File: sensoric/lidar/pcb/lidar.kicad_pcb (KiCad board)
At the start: 2 copper layers, 51.4 x 48.3 mm, 19 parts, among them J1 TWI, J2 TFMini-Plus, J3 28BYJ-48, SW1 SW_Push, U1 ATmega8L-8PU, U2 ULN2003A, Y1 16 MHz

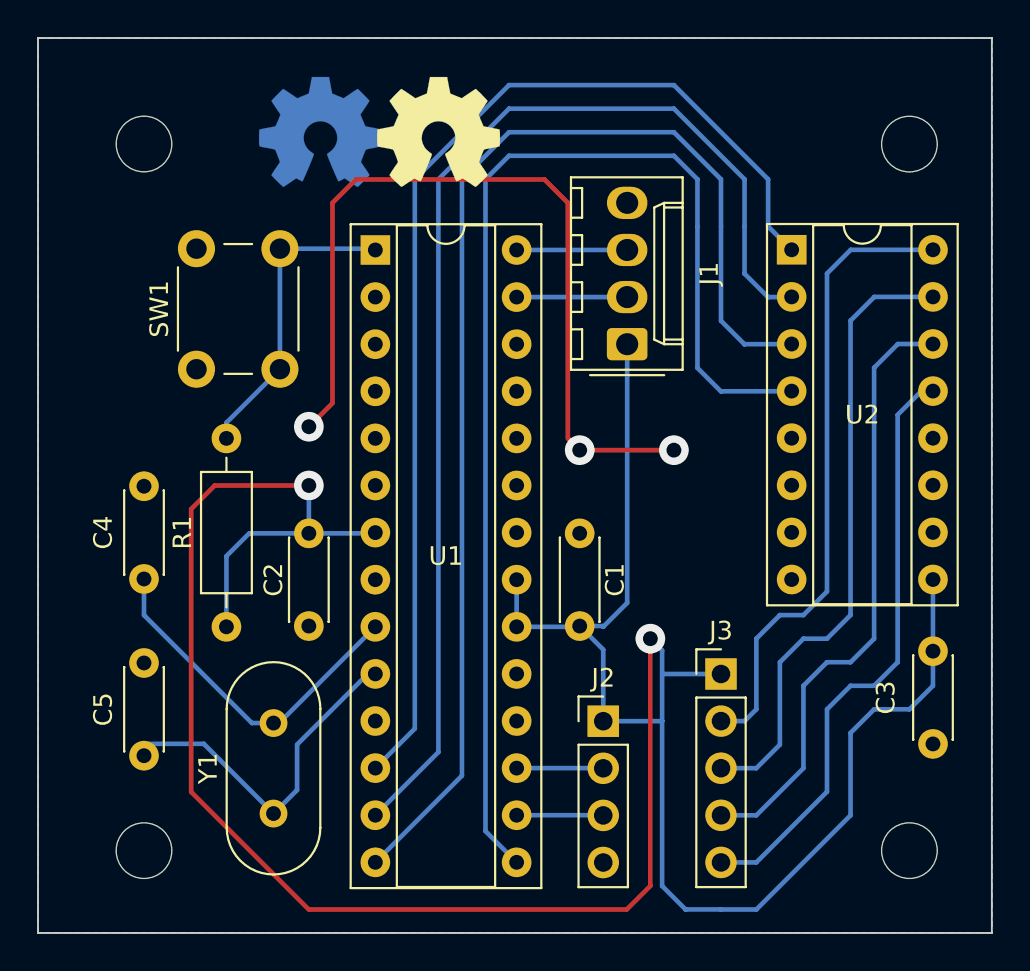
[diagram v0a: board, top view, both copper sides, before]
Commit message: refactor: moved from stepper motor to servo
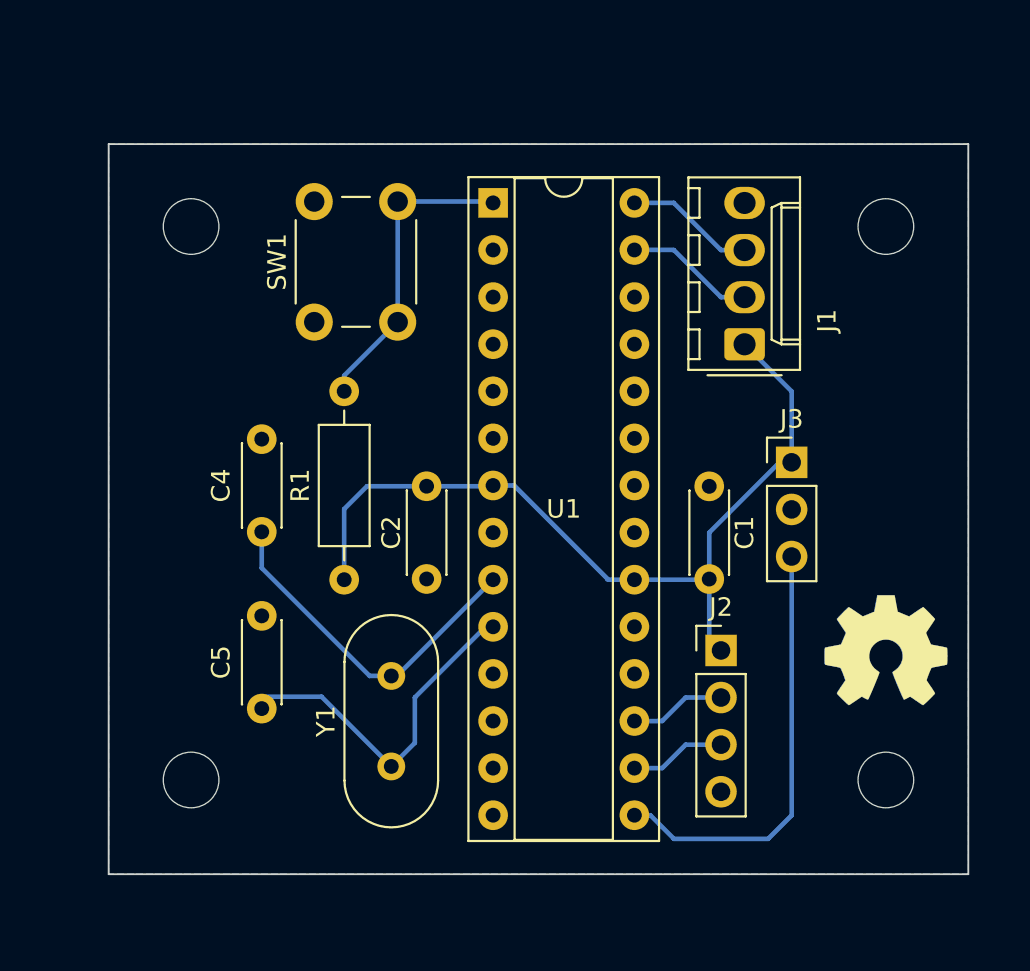
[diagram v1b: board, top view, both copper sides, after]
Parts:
- removed C3: 100 nF, Capacitor_THT:C_Disc_D4.3mm_W1.9mm_P5.00mm
- removed U2: ULN2003A, Package_DIP:DIP-16_W7.62mm_Socket
- J3: value 28BYJ-48 -> Servo SG90; footprint Connector_PinHeader_2.54mm:PinHeader_1x05_P2.54mm_Vertical -> Connector_PinHeader_2.54mm:PinHeader_1x03_P2.54mm_Vertical
- moved OSHW - copper 41.4 mm to (95.2, 95.2)
- moved OSHW - silk 36.9 mm to (95.2, 95.2)
- moved J3 12.0 mm to (90.2, 85.1)
- moved C1 7.43 mm to (85.7, 91.4)
- moved J2 7.41 mm to (86.4, 95.2)
- moved R1 6.84 mm to (66.0, 91.4)
- moved Y1 6.84 mm to (68.6, 101.5)
- moved C4 6.84 mm to (61.6, 88.9)
- moved C5 6.84 mm to (61.6, 98.4)
- moved C2 6.84 mm to (70.5, 86.4)
- moved U1 6.84 mm to (74.1, 71.1)
- moved SW1 6.84 mm to (64.4, 77.5)
- moved J1 6.33 mm to (87.6, 78.7)
- moved REF1 5.12 mm to (57.8, 72.4)
- moved REF2 4.62 mm to (95.2, 72.4)
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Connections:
- J3 pad 2: Net-(J3-Pad2) -> GND
- J3 pad 3: Net-(J3-Pad3) -> Net-(U1-Pad15)
- U1 pad 12: Net-(U1-Pad12) -> unconnected-(U1-Pad12)
- U1 pad 13: Net-(U1-Pad13) -> unconnected-(U1-Pad13)
- U1 pad 14: Net-(U1-Pad14) -> unconnected-(U1-Pad14)
- U1 pad 21: +5V -> unconnected-(U1-Pad21)
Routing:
- net +5V: track 155.4 -> 46.1 mm, vias 2 -> 0
- net Net-(U1-Pad14): track 66.8 -> 0.00 mm
- net Net-(U1-Pad13): track 63.5 -> 0.00 mm
- net Net-(U1-Pad12): track 60.2 -> 0.00 mm
- net GND: track 45.0 -> 0.00 mm, vias 3 -> 0
- net Net-(U1-Pad15): track 65.8 -> 23.5 mm
- net Net-(J3-Pad2): track 34.2 -> 0.00 mm
- net Net-(J3-Pad3): track 33.9 -> 0.00 mm
- net Net-(J3-Pad4): track 33.1 -> 0.00 mm
- net Net-(J3-Pad5): track 32.4 -> 0.00 mm
- net Net-(J1-Pad3): track 5.96 -> 6.99 mm
- net Net-(J1-Pad2): track 5.96 -> 6.99 mm
- net Net-(J2-Pad3): track 4.67 -> 5.19 mm
- net Net-(J2-Pad2): track 4.67 -> 5.19 mm
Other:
- board size 51.4 x 48.3 mm -> 46.4 x 39.4 mm
